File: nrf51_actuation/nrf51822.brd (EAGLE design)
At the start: 58 x 58 mm, 39 parts, among them T1 MMUN2238

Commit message: Small changes
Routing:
- net AIN1/XL1: track 25.9 -> 23.6 mm
- net N$3: track 27.8 -> 25.7 mm
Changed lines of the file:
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@@
 <vertex x="33.43148125" y="38.56228125"/>
 </polygon>
-<via x="39.49888125" y="9.16968125" extent="1-16" drill="0.6"/>
+<via x="38.50828125" y="8.91568125" extent="1-16" drill="0.6"/>
 <via x="22.89368125" y="9.02048125" extent="1-16" drill="0.6"/>
 <via x="19.89328125" y="18.39468125" extent="1-16" drill="0.6"/>
@@
 <wire x1="35.890540625" y1="17.406621875" x2="36.030903125" y2="17.3196" width="0.4064" layer="1"/>
 <wire x1="42.67808125" y1="15.97848125" x2="41.25568125" y2="17.40088125" width="1.27" layer="1"/>
-<wire x1="42.67808125" y1="15.97848125" x2="42.67808125" y2="4.80268125" width="1.27" layer="1"/>
-<wire x1="42.67808125" y1="4.80268125" x2="34.88088125" y2="1.70548125" width="1.27" layer="1"/>
+<wire x1="42.67808125" y1="15.97848125" x2="42.67808125" y2="9.50268125" width="1.27" layer="1"/>
+<wire x1="42.67808125" y1="9.50268125" x2="34.88088125" y2="1.70548125" width="1.27" layer="1"/>
 </signal>
 <signal name="N$4">
@@
 <wire x1="28.0162" y1="20.5486" x2="27.9654" y2="20.5486" width="0.3048" layer="1"/>
 <wire x1="27.9654" y1="20.5486" x2="27.8892" y2="20.6248" width="0.3048" layer="1"/>
-<wire x1="27.3558" y1="25.9842" x2="27.3558" y2="30.988" width="0.6096" layer="1"/>
-<wire x1="27.3558" y1="30.988" x2="27.3304" y2="30.9372" width="0.6096" layer="1"/>
 <wire x1="27.8892" y1="20.6248" x2="26.1874" y2="20.6248" width="0.3048" layer="1"/>
 <wire x1="26.1874" y1="20.6248" x2="25.8826" y2="20.9296" width="0.3048" layer="1"/>
@@
 <wire x1="25.8826" y1="20.955" x2="25.8826" y2="24.511" width="0.6096" layer="1"/>
 <wire x1="25.8826" y1="24.511" x2="27.3558" y2="25.9842" width="0.6096" layer="1"/>
-<wire x1="23.3426" y1="31.0134" x2="24.6634" y2="31.0134" width="0.6096" layer="1"/>
-<wire x1="24.6634" y1="31.0134" x2="27.3304" y2="31.0134" width="0.6096" layer="1"/>
-<wire x1="27.3304" y1="31.0134" x2="27.3558" y2="30.988" width="0.6096" layer="1"/>
-<wire x1="24.511" y1="31.1658" x2="24.6634" y2="31.0134" width="0.6096" layer="1"/>
 <contactref element="SJ1" pad="2"/>
-<wire x1="23.3426" y1="31.0134" x2="23.3426" y2="31.242" width="0.6096" layer="1"/>
-<wire x1="23.3426" y1="31.242" x2="22.0599" y2="32.5247" width="0.6096" layer="1"/>
-<wire x1="22.0599" y1="32.5247" x2="20.2946" y2="34.29" width="0.6096" layer="1"/>
-<wire x1="20.2946" y1="34.29" x2="19.558" y2="34.29" width="0.6096" layer="1"/>
-<wire x1="19.558" y1="34.29" x2="19.5326" y2="34.2646" width="0.6096" layer="1"/>
-<wire x1="22.733" y1="34.6202" x2="22.733" y2="33.1978" width="0.6096" layer="1"/>
-<wire x1="22.733" y1="33.1978" x2="22.0599" y2="32.5247" width="0.6096" layer="1"/>
+<wire x1="27.3558" y1="25.9842" x2="27.3558" y2="29.4132" width="0.6096" layer="1"/>
+<wire x1="27.3558" y1="29.4132" x2="25.7048" y2="31.0642" width="0.6096" layer="1"/>
+<wire x1="25.7048" y1="31.0642" x2="24.4856" y2="31.0642" width="0.6096" layer="1"/>
+<wire x1="24.4856" y1="31.0642" x2="22.733" y2="32.8168" width="0.6096" layer="1"/>
+<wire x1="22.733" y1="32.8168" x2="22.733" y2="34.6202" width="0.6096" layer="1"/>
+<wire x1="19.5326" y1="34.2646" x2="22.3774" y2="34.2646" width="0.6096" layer="1"/>
+<wire x1="22.3774" y1="34.2646" x2="22.733" y2="34.6202" width="0.6096" layer="1"/>
 </signal>
 <signal name="AIN6">

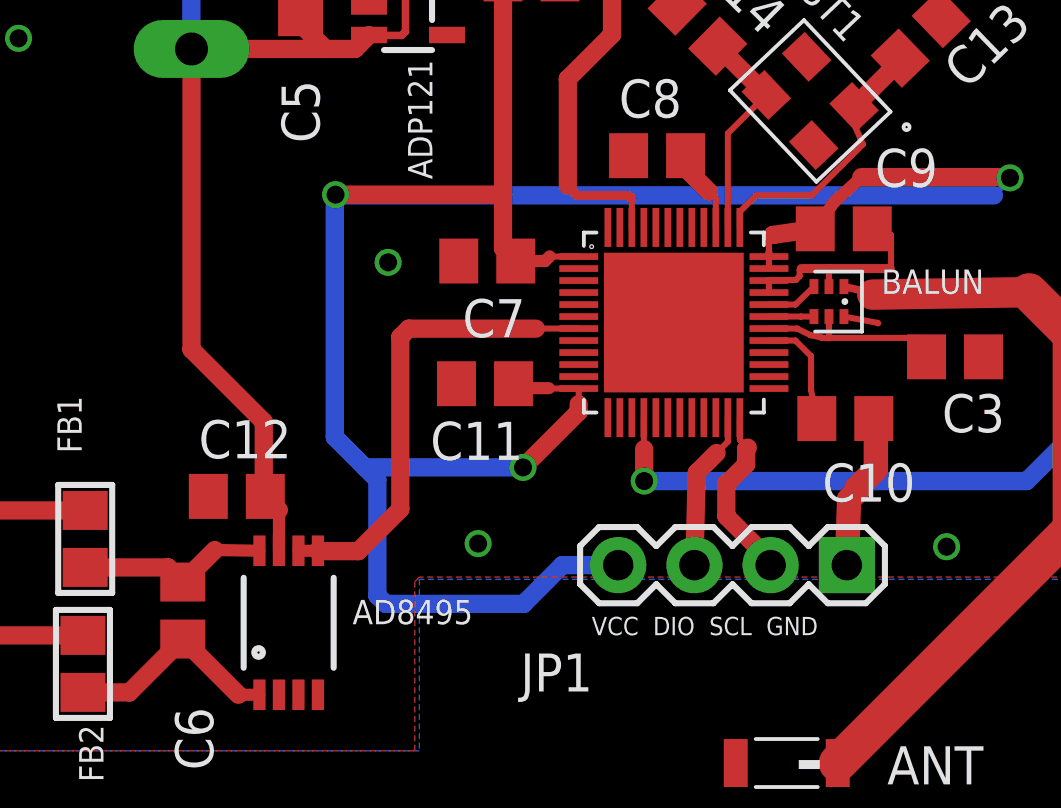
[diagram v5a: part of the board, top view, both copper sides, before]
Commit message: Added a TMP36 sensor to ensure a power cutoff if the temperature rises above a threshold (in case of fire or shortcut)
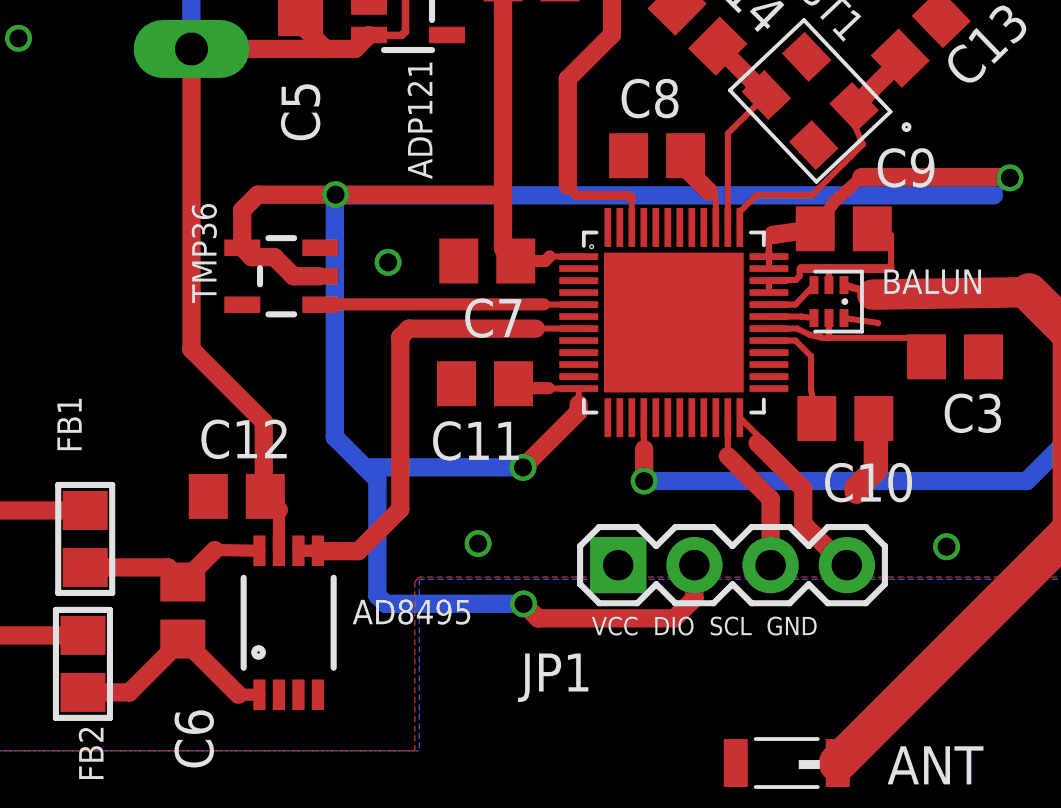
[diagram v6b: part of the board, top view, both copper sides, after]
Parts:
- added TMP36: TMP36_SOT23_5, NordicSemi:SOT23-5
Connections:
- net AIN2: now also TMP36.1
- net GND: now also JP1.1, TMP36.5; no longer JP1.4
- net N$12: now also JP1.3; no longer JP1.2
- net N$14: now also JP1.4; no longer JP1.3
- net VDD: now also JP1.2, TMP36.2, TMP36.4; no longer JP1.1
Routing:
- net VDD: track 90.5 -> 101.7 mm, vias 3 -> 4
- net AIN2: track 0.00 -> 8.63 mm
- net GND: track 14.1 -> 11.4 mm
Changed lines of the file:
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@@
 <element name="D2" library="microbuilder" package="DO-1N4148" value="" x="26.0604" y="38.5318"/>
 <element name="SJ1" library="microbuilder" package="SOLDERJUMPER_REFLOW_NOPASTE" value="SOLDERJUMPERREFLOW_NOPASTE" x="19.5326" y="35.0266" rot="R270"/>
+<element name="TMP36" library="NordicSemi" package="SOT23-5" value="TMP36_SOT23_5" x="16.3322" y="17.9324" rot="R90"/>
 </elements>
 <signals>
@@
 <contactref element="C7" pad="2"/>
 <contactref element="BALUN" pad="GND1"/>
-<contactref element="JP1" pad="4"/>
 <contactref element="C14" pad="1"/>
 <contactref element="C13" pad="1"/>
 <wire x1="32.58748125" y1="17.38808125" x2="32.58748125" y2="17.78808125" width="0.2032" layer="1"/>
-<wire x1="35.0885375" y1="16.586959375" x2="36.20728125" y2="16.37868125" width="0.2032" layer="1"/>
+<wire x1="35.0885375" y1="16.536959375" x2="36.20728125" y2="16.37868125" width="0.2032" layer="1"/>
 <wire x1="36.20728125" y1="16.37868125" x2="36.22648125" y2="16.35948125" width="0.2032" layer="1"/>
 <wire x1="32.58748125" y1="17.38808125" x2="32.58748125" y2="17.78868125" width="0.2032" layer="1"/>
@@
 <wire x1="36.65828125" y1="18.16288125" x2="36.65828125" y2="19.30068125" width="0.2032" layer="1"/>
 <wire x1="36.65828125" y1="19.30068125" x2="36.03168125" y2="19.51228125" width="0.2032" layer="1"/>
-<wire x1="34.5885375" y1="17.586959375" x2="34.5885375" y2="18.1759375" width="0.2032" layer="1"/>
+<wire x1="34.5885375" y1="17.636959375" x2="34.5885375" y2="18.1759375" width="0.2032" layer="1"/>
 <wire x1="34.5885375" y1="18.1759375" x2="34.60088125" y2="18.18828125" width="0.2032" layer="1"/>
-<wire x1="35.18328125" y1="8.30168125" x2="35.25948125" y2="10.49028125" width="0.8128" layer="1"/>
-<wire x1="35.25948125" y1="10.49028125" x2="35.51528125" y2="10.74608125" width="0.8128" layer="1"/>
 <wire x1="35.51528125" y1="10.74608125" x2="35.51528125" y2="10.87308125" width="0.8128" layer="1"/>
 <wire x1="35.51528125" y1="10.87308125" x2="36.15028125" y2="11.50808125" width="0.8128" layer="1"/>
@@
 <via x="20.09648125" y="31.34868125" extent="1-16" drill="0.6"/>
 <contactref element="C15" pad="2"/>
+<contactref element="TMP36" pad="5"/>
+<contactref element="JP1" pad="1"/>
 </signal>
 <signal name="VDD">
@@
 <contactref element="U$4" pad="35"/>
 <contactref element="U$4" pad="36"/>
-<contactref element="JP1" pad="1"/>
 <wire x1="21.85658125" y1="27.87268125" x2="23.72268125" y2="27.84208125" width="0.6096" layer="1"/>
 <wire x1="26.24748125" y1="18.58808125" x2="25.28568125" y2="18.58808125" width="0.2032" layer="1"/>
@@
 <wire x1="18.11628125" y1="20.62668125" x2="18.11628125" y2="12.5688" width="0.6096" layer="16"/>
 <wire x1="18.11628125" y1="12.5688" x2="19.1262" y2="11.55888125" width="0.6096" layer="16"/>
-<wire x1="27.56328125" y1="8.30168125" x2="25.70068125" y2="8.30168125" width="0.6096" layer="16"/>
-<wire x1="25.70068125" y1="8.30168125" x2="24.4094" y2="7.0104" width="0.6096" layer="16"/>
-<wire x1="24.4094" y1="7.0104" x2="19.812" y2="7.0104" width="0.6096" layer="16"/>
+<wire x1="23.4696" y1="7.0104" x2="19.812" y2="7.0104" width="0.6096" layer="16"/>
 <wire x1="19.812" y1="7.0104" x2="19.5326" y2="7.2898" width="0.6096" layer="16"/>
 <wire x1="19.5326" y1="7.2898" x2="19.5326" y2="11.15248125" width="0.6096" layer="16"/>
+<contactref element="TMP36" pad="2"/>
+<contactref element="TMP36" pad="4"/>
+<wire x1="15.0321" y1="18.8824" x2="15.0321" y2="20.1375" width="0.6096" layer="1"/>
+<wire x1="15.0321" y1="20.1375" x2="15.5448" y2="20.6502" width="0.6096" layer="1"/>
+<wire x1="15.5448" y1="20.6502" x2="18.1398" y2="20.6502" width="0.6096" layer="1"/>
+<wire x1="18.1398" y1="20.6502" x2="18.14168125" y2="20.65208125" width="0.6096" layer="1"/>
+<wire x1="17.6323" y1="17.9324" x2="16.7386" y2="17.9324" width="0.6096" layer="1"/>
+<wire x1="16.7386" y1="17.9324" x2="16.1036" y2="18.5674" width="0.6096" layer="1"/>
+<wire x1="16.1036" y1="18.5674" x2="15.3471" y2="18.5674" width="0.6096" layer="1"/>
+<wire x1="15.3471" y1="18.5674" x2="15.0321" y2="18.8824" width="0.6096" layer="1"/>
+<contactref element="JP1" pad="2"/>
+<wire x1="30.10328125" y1="8.30168125" x2="30.10328125" y2="7.19248125" width="0.6096" layer="1"/>
+<wire x1="30.10328125" y1="7.19248125" x2="29.4386" y2="6.5278" width="0.6096" layer="1"/>
+<wire x1="29.4386" y1="6.5278" x2="24.892" y2="6.5278" width="0.6096" layer="1"/>
+<wire x1="24.892" y1="6.5278" x2="24.4094" y2="7.0104" width="0.6096" layer="1"/>
+<via x="24.4094" y="7.0104" extent="1-16" drill="0.6"/>
+<wire x1="24.4094" y1="7.0104" x2="23.4696" y2="7.0104" width="0.6096" layer="16"/>
 </signal>
 <signal name="AIN4">
@@
 <contactref element="BALUN" pad="BAL1"/>
 <wire x1="32.58748125" y1="16.98808125" x2="33.47188125" y2="16.98808125" width="0.2032" layer="1"/>
-<wire x1="33.47188125" y1="16.98808125" x2="34.0885375" y2="17.586959375" width="0.2032" layer="1"/>
+<wire x1="33.47188125" y1="16.98808125" x2="34.0885375" y2="17.636959375" width="0.2032" layer="1"/>
 </signal>
 <signal name="N$13">
@@
 <contactref element="BALUN" pad="BAL2"/>
 <wire x1="32.58748125" y1="16.58808125" x2="33.65308125" y2="16.58808125" width="0.2032" layer="1"/>
-<wire x1="33.65308125" y1="16.58808125" x2="34.0885375" y2="16.586959375" width="0.2032" layer="1"/>
+<wire x1="33.65308125" y1="16.58808125" x2="34.0885375" y2="16.536959375" width="0.2032" layer="1"/>
 </signal>
 <signal name="N$3">
@@
 <contactref element="BALUN" pad="UBAL"/>
 <wire x1="41.25568125" y1="17.40088125" x2="36.030903125" y2="17.3196" width="1.016" layer="1"/>
-<wire x1="35.0885375" y1="17.586959375" x2="35.890540625" y2="17.406621875" width="0.254" layer="1"/>
+<wire x1="35.0885375" y1="17.636959375" x2="35.890540625" y2="17.406621875" width="0.254" layer="1"/>
 <wire x1="35.890540625" y1="17.406621875" x2="36.030903125" y2="17.3196" width="0.4064" layer="1"/>
 <wire x1="42.67808125" y1="15.97848125" x2="41.25568125" y2="17.40088125" width="1.27" layer="1"/>
@@
 <wire x1="34.34688125" y1="15.87688125" x2="37.61468125" y2="15.87688125" width="0.2032" layer="1"/>
 <wire x1="37.61468125" y1="15.87688125" x2="37.84008125" y2="15.24508125" width="0.2032" layer="1"/>
-<wire x1="34.5885375" y1="16.586959375" x2="34.59108125" y2="15.86708125" width="0.2032" layer="1"/>
+<wire x1="34.5885375" y1="16.536959375" x2="34.59108125" y2="15.86708125" width="0.2032" layer="1"/>
 <wire x1="34.59108125" y1="15.86708125" x2="34.34688125" y2="15.87688125" width="0.2032" layer="1"/>
 <wire x1="32.58748125" y1="16.18808125" x2="33.525140625" y2="16.18808125" width="0.2032" layer="1"/>
@@
 <signal name="AIN2">
 <contactref element="U$4" pad="5"/>
+<contactref element="TMP36" pad="1"/>
+<wire x1="17.6323" y1="16.98808125" x2="17.6323" y2="16.9824" width="0.2032" layer="1"/>
+<wire x1="26.24748125" y1="16.98808125" x2="25.09971875" y2="16.98808125" width="0.2032" layer="1"/>
+<wire x1="25.09971875" y1="16.98808125" x2="25.0952" y2="16.9926" width="0.2032" layer="1"/>
+<wire x1="25.0952" y1="16.9926" x2="17.6425" y2="16.9926" width="0.4064" layer="1"/>
+<wire x1="17.6425" y1="16.9926" x2="17.6323" y2="16.9824" width="0.4064" layer="1"/>
 </signal>
 <signal name="AIN3">
@@
 <signal name="N$12">
 <contactref element="U$4" pad="23"/>
-<contactref element="JP1" pad="2"/>
-<wire x1="31.21748125" y1="13.21808125" x2="31.21748125" y2="12.41728125" width="0.2032" layer="1"/>
-<wire x1="31.21748125" y1="12.41728125" x2="30.84168125" y2="12.04148125" width="0.2032" layer="1"/>
-<wire x1="30.10328125" y1="8.30168125" x2="30.17948125" y2="11.37928125" width="0.6096" layer="1"/>
-<wire x1="30.17948125" y1="11.37928125" x2="30.84168125" y2="12.04148125" width="0.6096" layer="1"/>
+<contactref element="JP1" pad="3"/>
+<wire x1="32.64328125" y1="8.30168125" x2="32.64328125" y2="10.51131875" width="0.6096" layer="1"/>
+<wire x1="32.64328125" y1="10.51131875" x2="31.2166" y2="11.938" width="0.6096" layer="1"/>
+<wire x1="31.2166" y1="11.938" x2="31.2166" y2="13.2172" width="0.2032" layer="1"/>
+<wire x1="31.2166" y1="13.2172" x2="31.21748125" y2="13.21808125" width="0.2032" layer="1"/>
 </signal>
 <signal name="N$14">
 <contactref element="U$4" pad="24"/>
-<contactref element="JP1" pad="3"/>
-<wire x1="31.61748125" y1="13.21808125" x2="31.61748125" y2="12.48488125" width="0.2032" layer="1"/>
-<wire x1="31.61748125" y1="12.48488125" x2="31.88308125" y2="12.21928125" width="0.2032" layer="1"/>
-<wire x1="32.64328125" y1="8.30168125" x2="32.64328125" y2="8.45391875" width="0.6096" layer="1"/>
-<wire x1="32.64328125" y1="8.45391875" x2="31.1658" y2="9.9314" width="0.6096" layer="1"/>
-<wire x1="31.1658" y1="9.9314" x2="31.1658" y2="11.0236" width="0.6096" layer="1"/>
-<wire x1="31.1658" y1="11.0236" x2="31.1912" y2="11.049" width="0.6096" layer="1"/>
-<wire x1="31.1912" y1="11.049" x2="31.2166" y2="11.049" width="0.6096" layer="1"/>
-<wire x1="31.2166" y1="11.049" x2="31.8262" y2="11.6586" width="0.6096" layer="1"/>
-<wire x1="31.8262" y1="11.6586" x2="31.8262" y2="12.1624" width="0.6096" layer="1"/>
-<wire x1="31.8262" y1="12.1624" x2="31.88308125" y2="12.21928125" width="0.6096" layer="1"/>
+<contactref element="JP1" pad="4"/>
+<wire x1="35.18328125" y1="8.30168125" x2="35.10691875" y2="8.30168125" width="0.6096" layer="1"/>
+<wire x1="35.10691875" y1="8.30168125" x2="33.7312" y2="9.6774" width="0.6096" layer="1"/>
+<wire x1="33.7312" y1="9.6774" x2="33.7312" y2="10.8458" width="0.6096" layer="1"/>
+<wire x1="33.7312" y1="10.8458" x2="32.2072" y2="12.3698" width="0.6096" layer="1"/>
+<wire x1="32.2072" y1="12.3698" x2="32.2072" y2="12.6283625" width="0.2032" layer="1"/>
+<wire x1="32.2072" y1="12.6283625" x2="31.61748125" y2="13.21808125" width="0.2032" layer="1"/>
 </signal>
 <signal name="GIOP9">

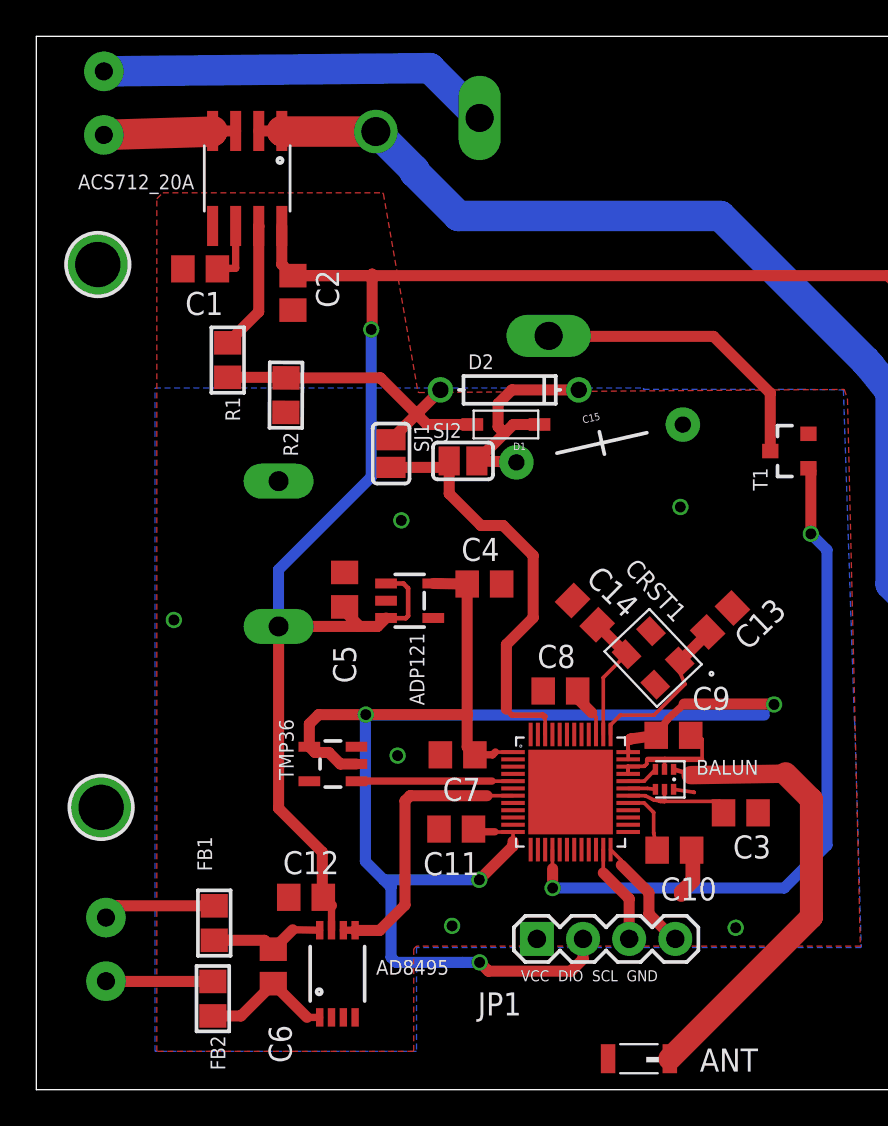
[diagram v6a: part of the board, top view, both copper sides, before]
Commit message: Cleaned sensor board v.1.2 - TAG AS SENT TO SMART PROTOTYPE Cleaned actuation board v.1.0 - TAG AS SENT TO SMART PROTOTYPE Made a compact version of the sensor board - TAG AS SENT TO SMART PROTOTYPE
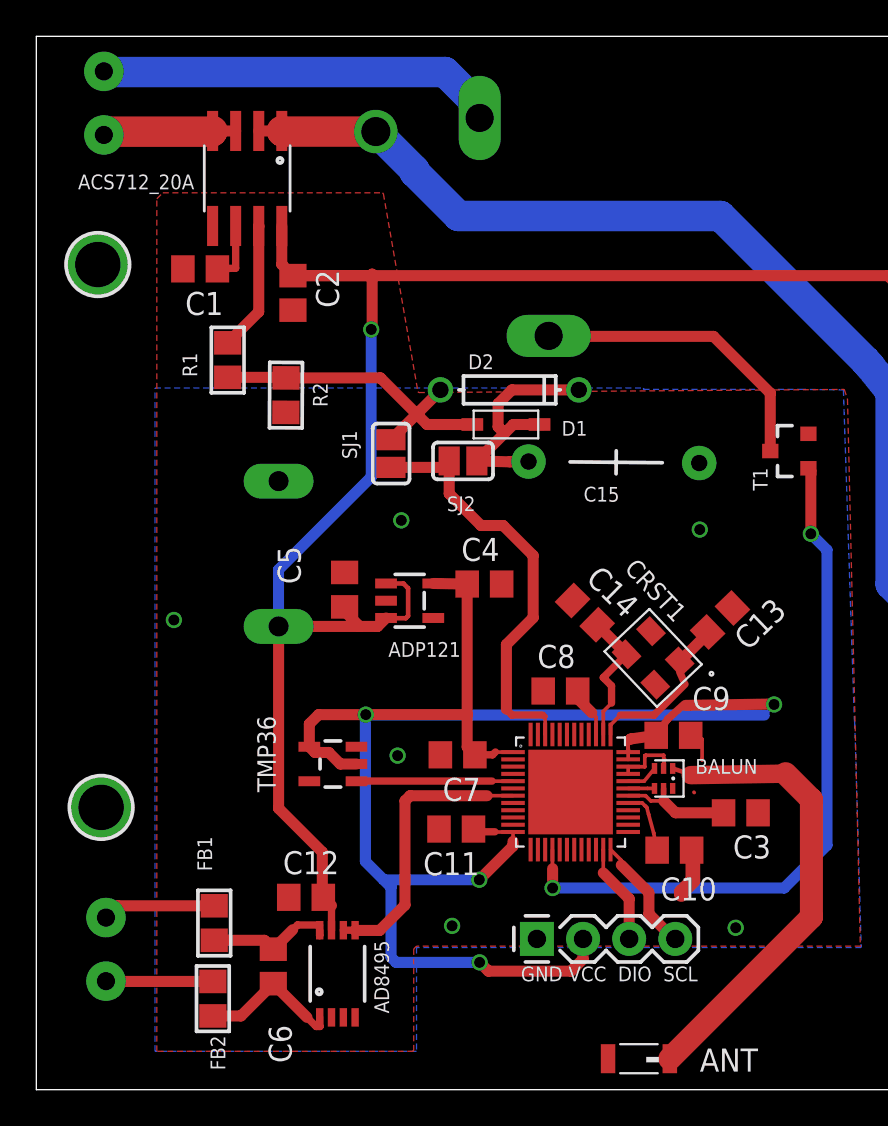
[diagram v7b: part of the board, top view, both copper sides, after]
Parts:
- moved C15 1.33 mm to (31.9, 34.5), turned to 359.5 degrees
- moved BALUN 0.07 mm to (34.0, 17.6)
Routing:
- net GND: track 11.4 -> 8.84 mm
- net N$9: track 6.45 -> 7.44 mm
- net N$16: track 7.39 -> 8.12 mm
- net N$19: track 13.3 -> 13.9 mm
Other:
- board text added: "GND VCC DIO SCL"
- board text removed: "VCC DIO SCL GND"
